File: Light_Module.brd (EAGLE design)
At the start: 63.5 x 88.9 mm, 67 parts, among them IC1 TLC59711, IC2 TLC59711

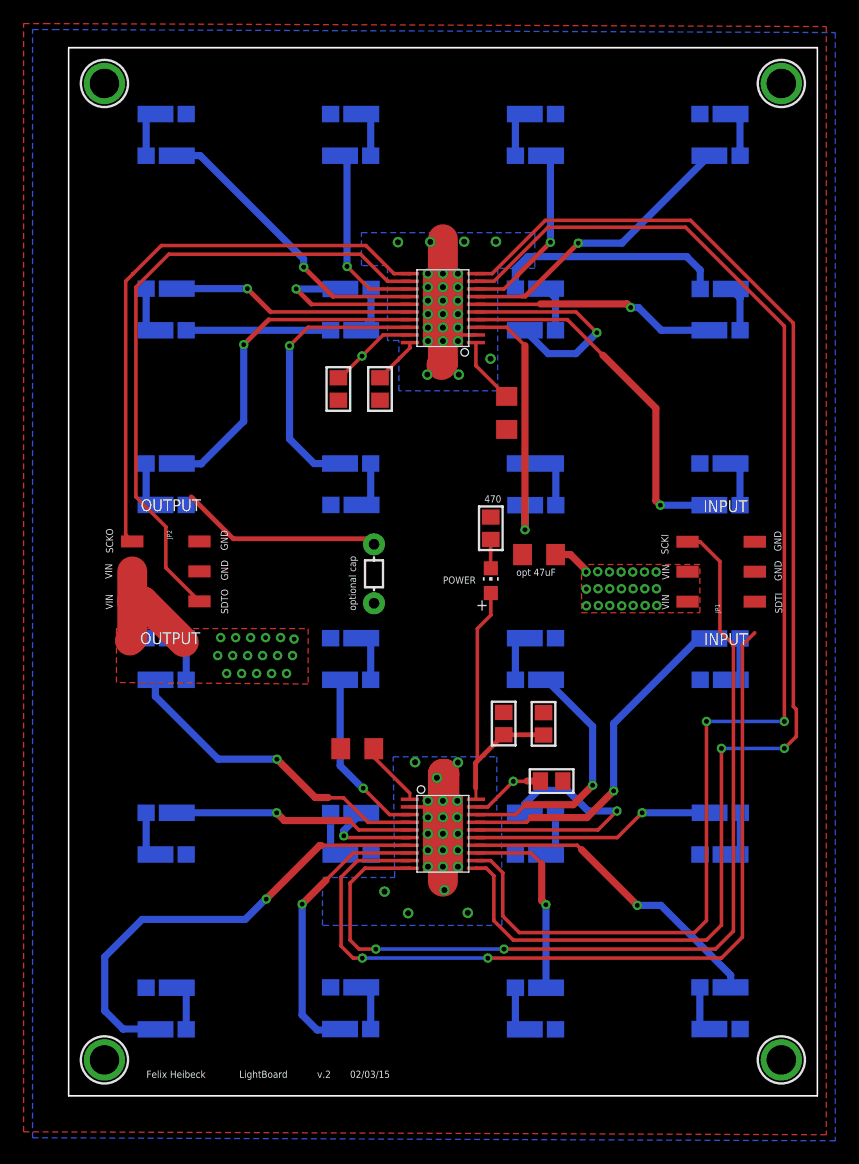
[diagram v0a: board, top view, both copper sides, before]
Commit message: small revision
delete v.1 - fix small missing connection
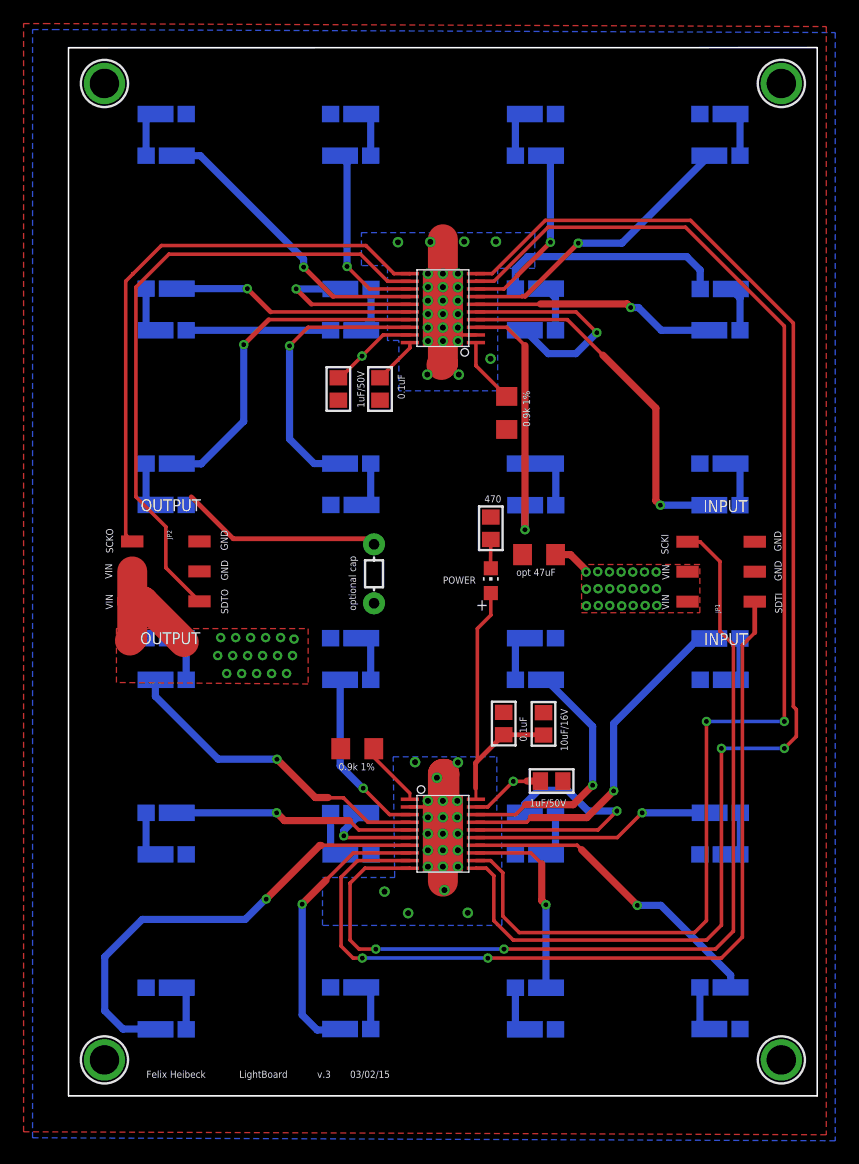
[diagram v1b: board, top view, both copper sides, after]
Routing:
- net SDTI: track 73.7 -> 76.3 mm
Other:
- board text added: "03/02/15"
- board text added: "v.3"
- board text removed: "02/03/15"
- board text removed: "v.2"
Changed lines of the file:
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@@
 <board>
 <plain>
-<wire x1="0" y1="0" x2="63.5054" y2="0" width="0" layer="20"/>
-<wire x1="63.5054" y1="0" x2="63.5054" y2="88.8748" width="0" layer="20"/>
-<wire x1="63.5054" y1="88.8748" x2="0" y2="88.8748" width="0" layer="20"/>
+<wire x1="0" y1="0" x2="63.5" y2="0" width="0" layer="20"/>
+<wire x1="63.5" y1="0" x2="63.5" y2="88.9" width="0" layer="20"/>
+<wire x1="63.5" y1="88.9" x2="0" y2="88.8748" width="0" layer="20"/>
 <wire x1="0" y1="88.8748" x2="0" y2="0" width="0" layer="20"/>
 <wire x1="11.709640625" y1="48.437790625" x2="4.85163125" y2="48.437790625" width="0" layer="22"/>
-<text x="39.0906" y="28.0924" size="0.6096" layer="27" font="vector" ratio="10">1uF/50V</text>
+<text x="39.0906" y="24.5364" size="0.6096" layer="25" font="vector" ratio="10">1uF/50V</text>
 <wire x1="11.70903125" y1="10.8457125" x2="11.70903125" y2="3.9877125" width="0" layer="26"/>
 <wire x1="11.70903125" y1="3.9877125" x2="4.851021875" y2="3.9877125" width="0" layer="26"/>
@@
 <wire x1="53.252621875" y1="6.3526625" x2="57.252621875" y2="6.3526625" width="0" layer="26"/>
 <wire x1="57.252621875" y1="6.3526625" x2="57.252621875" y2="4.9526625" width="0" layer="26"/>
-<wire x1="63.516321875" y1="88.90838125" x2="63.516321875" y2="0.008371875" width="0" layer="121"/>
-<wire x1="63.516321875" y1="0.008371875" x2="0.016321875" y2="0.008371875" width="0" layer="121"/>
-<wire x1="0.016321875" y1="0.008371875" x2="0.016321875" y2="88.90838125" width="0" layer="121"/>
-<wire x1="0.016321875" y1="88.90838125" x2="63.516321875" y2="88.90838125" width="0" layer="121"/>
+<wire x1="63.5" y1="88.9" x2="63.5" y2="0" width="0" layer="121"/>
+<wire x1="63.5" y1="0" x2="0" y2="0" width="0" layer="121"/>
+<wire x1="0" y1="0" x2="0" y2="88.9" width="0" layer="121"/>
+<wire x1="0" y1="88.9" x2="63.5" y2="88.9" width="0" layer="121"/>
 <text x="6.604" y="1.524" size="0.6096" layer="21" font="vector" ratio="10">Felix Heibeck</text>
 <text x="14.478" y="1.524" size="0.6096" layer="21" font="vector" ratio="10">LightBoard</text>
-<text x="21.082" y="1.524" size="0.6096" layer="21" font="vector" ratio="10">v.2</text>
-<text x="23.876" y="1.524" size="0.6096" layer="21" font="vector" ratio="10">02/03/15</text>
+<text x="21.082" y="1.524" size="0.6096" layer="21" font="vector" ratio="10">v.3</text>
+<text x="23.876" y="1.524" size="0.6096" layer="21" font="vector" ratio="10">03/02/15</text>
 <text x="36.703" y="50.927" size="0.6096" layer="21" font="vector" ratio="10" rot="R180">470</text>
 <text x="24.384" y="41.148" size="0.6096" layer="21" font="vector" ratio="10" rot="R90">optional cap</text>
@@
 <element name="U$4" library="microbuilder" package="MOUNTINGHOLE_2.5_PLATED" value="MOUNTINGHOLE2.5" x="60.452" y="85.852" smashed="yes"/>
 <element name="C1" library="microbuilder" package="0805" value="10uF/16V" x="40.2844" y="31.5468" smashed="yes" rot="R90">
-<attribute name="VALUE" x="42.0878" y="29.2354" size="0.6096" layer="27" font="vector" ratio="10" rot="R90"/>
+<attribute name="VALUE" x="42.3418" y="29.2354" size="0.6096" layer="25" font="vector" ratio="10" rot="R90"/>
 </element>
 <element name="C2" library="microbuilder" package="0805" value="1uF/50V" x="40.9702" y="26.6954" smashed="yes"/>
@@
 <element name="IC1" library="adafruit" package="HTSSOP20DAP" value="TLC59711" x="31.75" y="22.225" smashed="yes" rot="R270"/>
 <element name="R3" library="SparkFun-Passives" package="1206" value="0.9k 1%" x="24.4856" y="29.4386" smashed="yes" rot="R180">
-<attribute name="VALUE" x="22.9044" y="27.6034" size="0.6096" layer="27" font="vector" ratio="10"/>
+<attribute name="VALUE" x="22.9044" y="27.6034" size="0.6096" layer="25" font="vector" ratio="10"/>
 </element>
 <element name="IC2" library="adafruit" package="HTSSOP20DAP" value="TLC59711" x="31.75" y="66.802" smashed="yes" rot="R90"/>
 <element name="R1" library="SparkFun-Passives" package="1206" value="0.9k 1%" x="37.1602" y="57.912" smashed="yes" rot="R270">
-<attribute name="VALUE" x="38.5318" y="59.7916" size="0.6096" layer="27" ratio="10" rot="R270"/>
+<attribute name="VALUE" x="38.5318" y="59.7916" size="0.6096" layer="25" ratio="10" rot="R270"/>
 </element>
 <element name="C3" library="microbuilder" package="0805" value="1uF/50V" x="22.8854" y="59.944" smashed="yes" rot="R270">
-<attribute name="VALUE" x="24.4856" y="61.468" size="0.6096" layer="27" ratio="10" rot="R270"/>
+<attribute name="VALUE" x="24.4856" y="61.468" size="0.6096" layer="25" ratio="10" rot="R270"/>
 </element>
 <element name="C5" library="microbuilder" package="0805" value="0.1uF" x="36.9062" y="31.5722" smashed="yes" rot="R90">
-<attribute name="VALUE" x="38.862" y="30.0482" size="0.6096" layer="27" ratio="10" rot="R90"/>
+<attribute name="VALUE" x="38.862" y="30.0482" size="0.6096" layer="25" ratio="10" rot="R90"/>
 </element>
 <element name="C6" library="microbuilder" package="0805" value="0.1uF" x="26.416" y="59.944" smashed="yes" rot="R270">
-<attribute name="VALUE" x="27.9146" y="61.1886" size="0.6096" layer="27" ratio="10" rot="R270"/>
+<attribute name="VALUE" x="27.9146" y="61.1886" size="0.6096" layer="25" ratio="10" rot="R270"/>
 </element>
 <element name="LED4" library="digikey" package="DS205" value="" x="8.2296" y="38.8112" smashed="yes" rot="MR180">
@@
 <wire x1="58.1966" y1="39.2726" x2="57.15" y2="38.226" width="0.3048" layer="1"/>
 <contactref element="JP1" pad="1"/>
-<wire x1="58.1966" y1="39.2726" x2="58.1966" y2="41.91" width="0" layer="19" extent="1-1"/>
+<wire x1="58.1966" y1="41.91" x2="58.1966" y2="39.2726" width="0.4064" layer="1"/>
 </signal>
 <signal name="SCKI">

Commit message: delete some
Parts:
- removed LED27, LED29, LED31, LED33, LED35, LED37, LED39, LED41, LED43, LED45, LED47, LED49: (no value), digikey:DS205
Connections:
- removed net N$20: LED26.P$2, LED27.P$1
- removed net N$21: LED28.P$2, LED29.P$1
- removed net N$22: LED30.P$2, LED31.P$1
- removed net N$23: LED32.P$2, LED33.P$1
- removed net N$24: LED34.P$2, LED35.P$1
- removed net N$25: LED36.P$2, LED37.P$1
- removed net N$26: LED38.P$2, LED39.P$1
- removed net N$27: LED40.P$2, LED41.P$1
- removed net N$28: LED42.P$2, LED43.P$1
- removed net N$29: LED44.P$2, LED45.P$1
- removed net N$30: LED46.P$2, LED47.P$1
- removed net N$31: LED48.P$2, LED49.P$1
- net 2_0: now also LED28.P$2; no longer LED29.P$2
- net 2_1: now also LED26.P$2; no longer LED27.P$2
- net 2_10: now also LED46.P$2; no longer LED47.P$2
- net 2_11: now also LED48.P$2; no longer LED49.P$2
- net 2_2: now also LED32.P$2; no longer LED33.P$2
- net 2_3: now also LED30.P$2; no longer LED31.P$2
- net 2_4: now also LED34.P$2; no longer LED35.P$2
- net 2_5: now also LED36.P$2; no longer LED37.P$2
- net 2_6: now also LED38.P$2; no longer LED39.P$2
- net 2_7: now also LED40.P$2; no longer LED41.P$2
- net 2_8: now also LED42.P$2; no longer LED43.P$2
- net 2_9: now also LED44.P$2; no longer LED45.P$2
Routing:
- net 2_4: track 24.7 -> 14.3 mm
- net 2_9: track 20.6 -> 14.6 mm
- net N$31: track 4.43 -> 0.00 mm
- net N$26: track 4.41 -> 0.00 mm
- net N$24: track 4.39 -> 0.00 mm
- net N$29: track 4.34 -> 0.00 mm
- net N$20: track 4.31 -> 0.00 mm
- net N$27: track 4.30 -> 0.00 mm
- net N$21: track 4.30 -> 0.00 mm
- net N$30: track 4.28 -> 0.00 mm
- net N$25: track 4.24 -> 0.00 mm
- net 2_1: track 30.9 -> 26.8 mm
- net 2_3: track 20.7 -> 16.7 mm
- net N$23: track 3.86 -> 0.00 mm
- net N$28: track 3.85 -> 0.00 mm
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
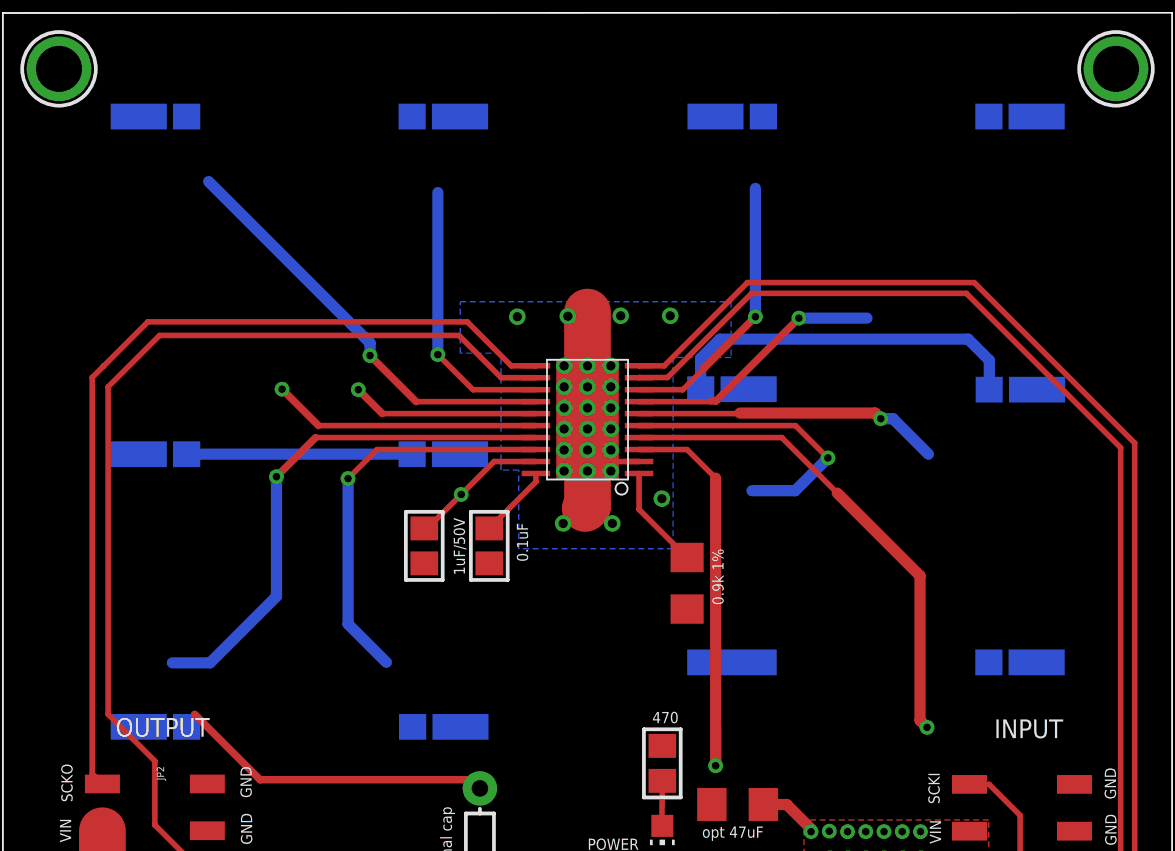
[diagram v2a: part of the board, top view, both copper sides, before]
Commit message: Revert 42a1a8e..717766d
This rolls back to commit 42a1a8ecaa921d949cbaf7c99d83dff5afafc410.
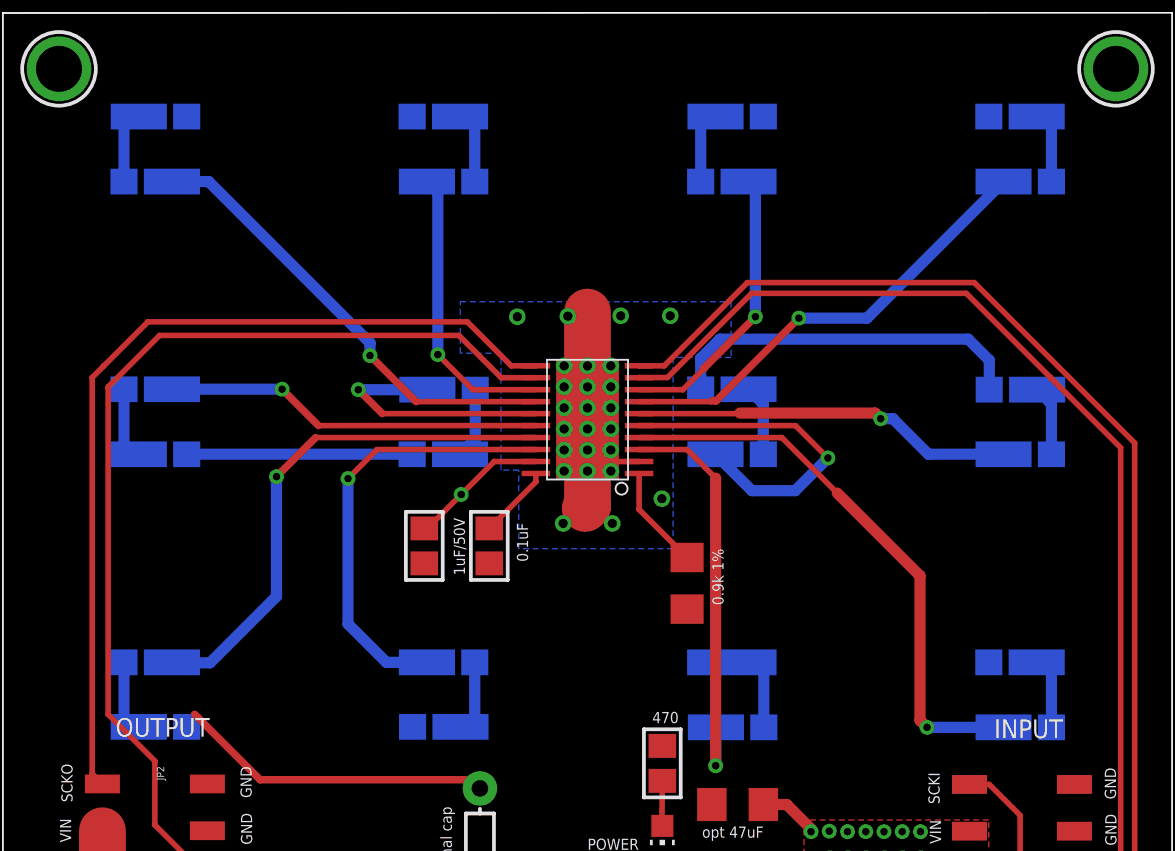
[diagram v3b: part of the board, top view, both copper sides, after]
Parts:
- added LED27, LED29, LED31, LED33, LED35, LED37, LED39, LED41, LED43, LED45, LED47, LED49: (no value), digikey:DS205
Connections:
- new net N$20: LED26.P$2, LED27.P$1
- new net N$21: LED28.P$2, LED29.P$1
- new net N$22: LED30.P$2, LED31.P$1
- new net N$23: LED32.P$2, LED33.P$1
- new net N$24: LED34.P$2, LED35.P$1
- new net N$25: LED36.P$2, LED37.P$1
- new net N$26: LED38.P$2, LED39.P$1
- new net N$27: LED40.P$2, LED41.P$1
- new net N$28: LED42.P$2, LED43.P$1
- new net N$29: LED44.P$2, LED45.P$1
- new net N$30: LED46.P$2, LED47.P$1
- new net N$31: LED48.P$2, LED49.P$1
- net 2_0: now also LED29.P$2; no longer LED28.P$2
- net 2_1: now also LED27.P$2; no longer LED26.P$2
- net 2_10: now also LED47.P$2; no longer LED46.P$2
- net 2_11: now also LED49.P$2; no longer LED48.P$2
- net 2_2: now also LED33.P$2; no longer LED32.P$2
- net 2_3: now also LED31.P$2; no longer LED30.P$2
- net 2_4: now also LED35.P$2; no longer LED34.P$2
- net 2_5: now also LED37.P$2; no longer LED36.P$2
- net 2_6: now also LED39.P$2; no longer LED38.P$2
- net 2_7: now also LED41.P$2; no longer LED40.P$2
- net 2_8: now also LED43.P$2; no longer LED42.P$2
- net 2_9: now also LED45.P$2; no longer LED44.P$2
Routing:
- net 2_4: track 14.3 -> 24.7 mm
- net 2_9: track 14.6 -> 20.6 mm
- net N$31: track 0.00 -> 4.43 mm
- net N$26: track 0.00 -> 4.41 mm
- net N$24: track 0.00 -> 4.39 mm
- net N$29: track 0.00 -> 4.34 mm
- net N$20: track 0.00 -> 4.31 mm
- net N$27: track 0.00 -> 4.30 mm
- net N$21: track 0.00 -> 4.30 mm
- net N$30: track 0.00 -> 4.28 mm
- net N$25: track 0.00 -> 4.24 mm
- net 2_1: track 26.8 -> 30.9 mm
- net 2_3: track 16.7 -> 20.7 mm
- net N$23: track 0.00 -> 3.86 mm
- net N$28: track 0.00 -> 3.85 mm
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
